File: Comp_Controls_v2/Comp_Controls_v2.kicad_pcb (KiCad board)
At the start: 2 copper layers, 78 x 108.9 mm, 39 parts

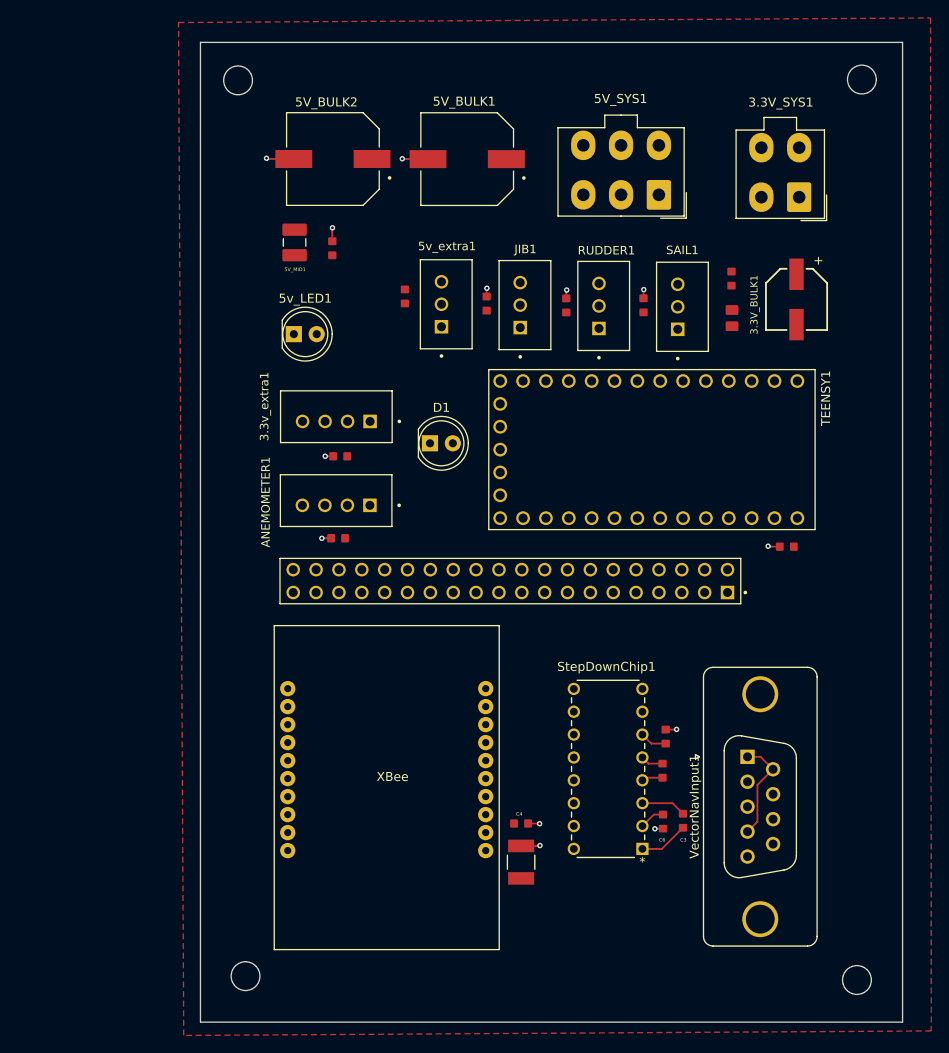
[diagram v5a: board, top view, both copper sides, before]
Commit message: rounded corners done
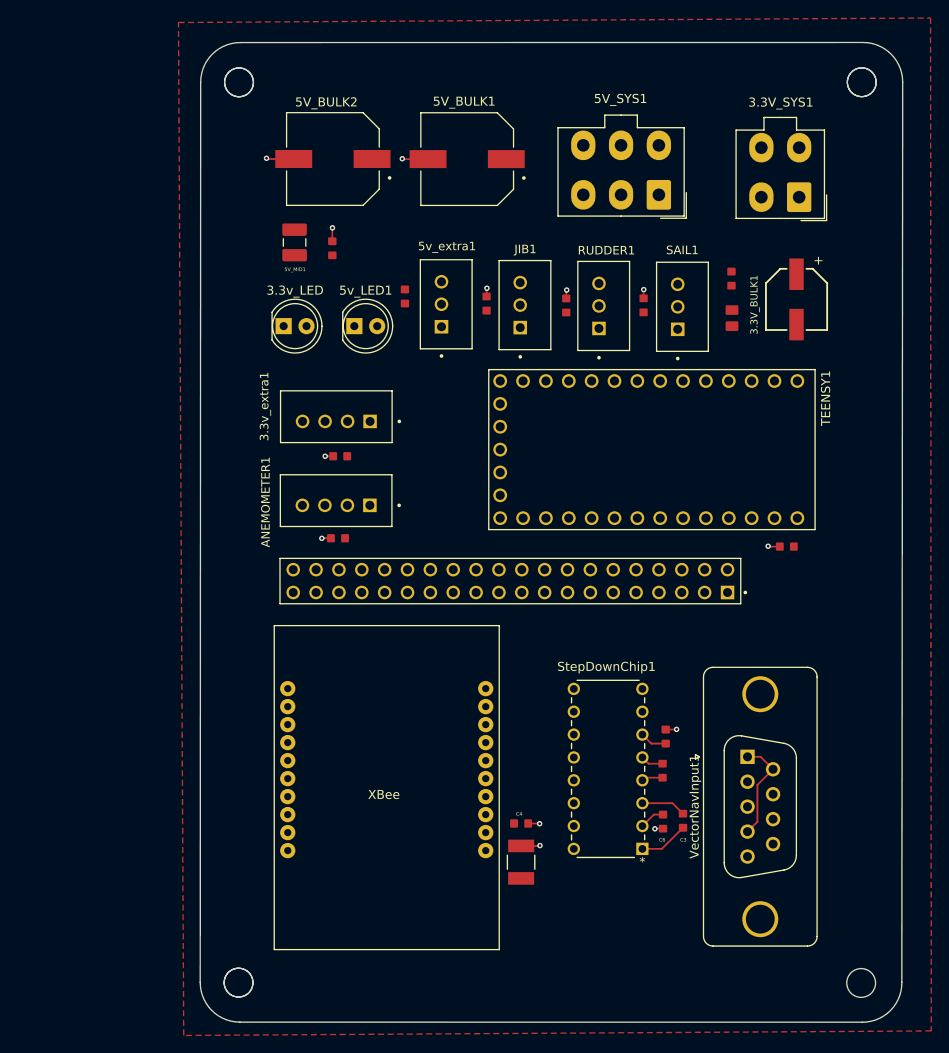
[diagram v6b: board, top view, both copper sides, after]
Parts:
- removed H2, H3, H4: MountingHole, MountingHole:MountingHole_3.2mm_M3
- added ?: , , F.Cu at (118.9, 39.5)
- added ?: , , F.Cu at (188.1, 39.5)
- added ?: , , F.Cu at (118.9, 139.5)
- added H1: MountingHole, MountingHole:MountingHole_3.2mm_M3, F.Cu at (118.9, 39.5)
- added H1: MountingHole, MountingHole:MountingHole_3.2mm_M3, F.Cu at (118.9, 139.5)
- added H1: MountingHole, MountingHole:MountingHole_3.2mm_M3, F.Cu at (188.1, 39.5)
- moved 3.3v_LED 20.8 mm to (123.9, 66.6)
- moved 5v_LED1 6.78 mm to (131.7, 66.6)
- moved H1 0.57 mm to (188.1, 139.6)
- renumbered D1 to 3.3v_LED
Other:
- board size 78 x 108.9 mm -> 78.1 x 108.9 mm

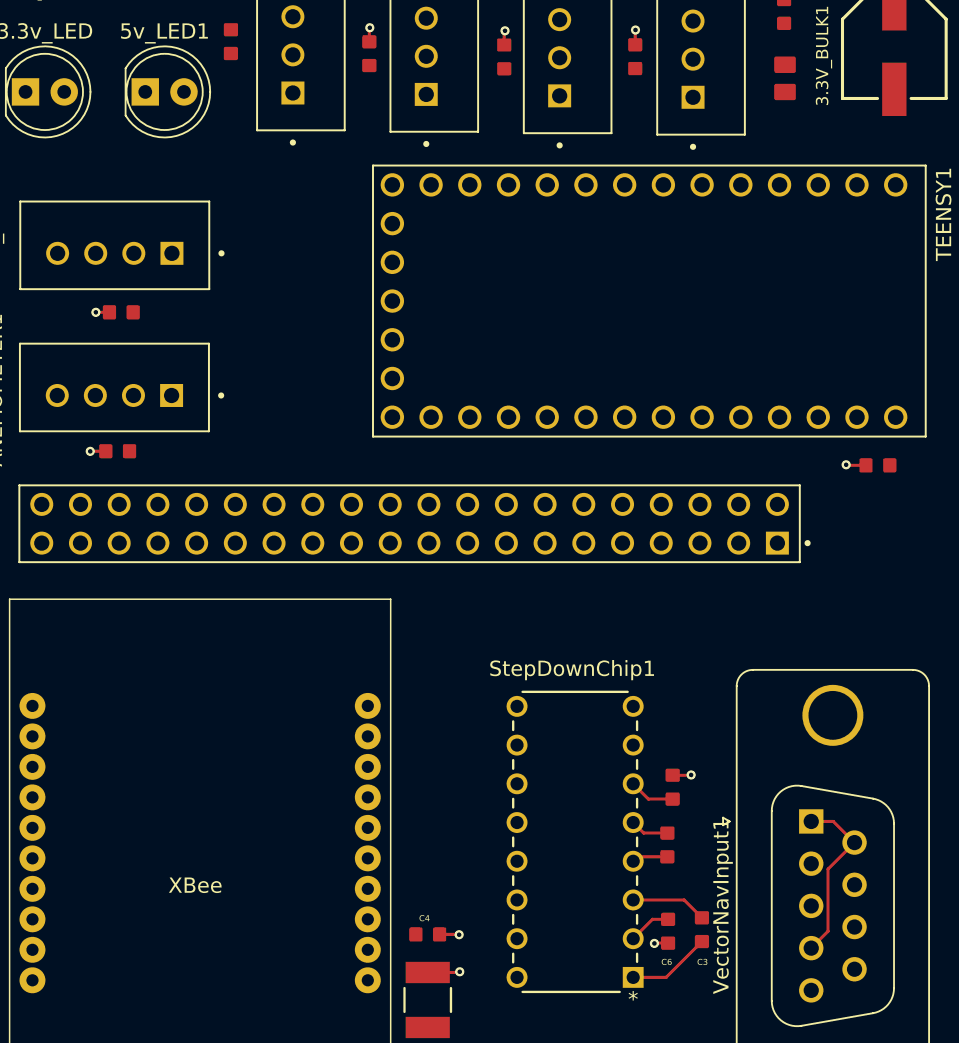
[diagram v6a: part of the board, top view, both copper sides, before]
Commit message: Add signal traces
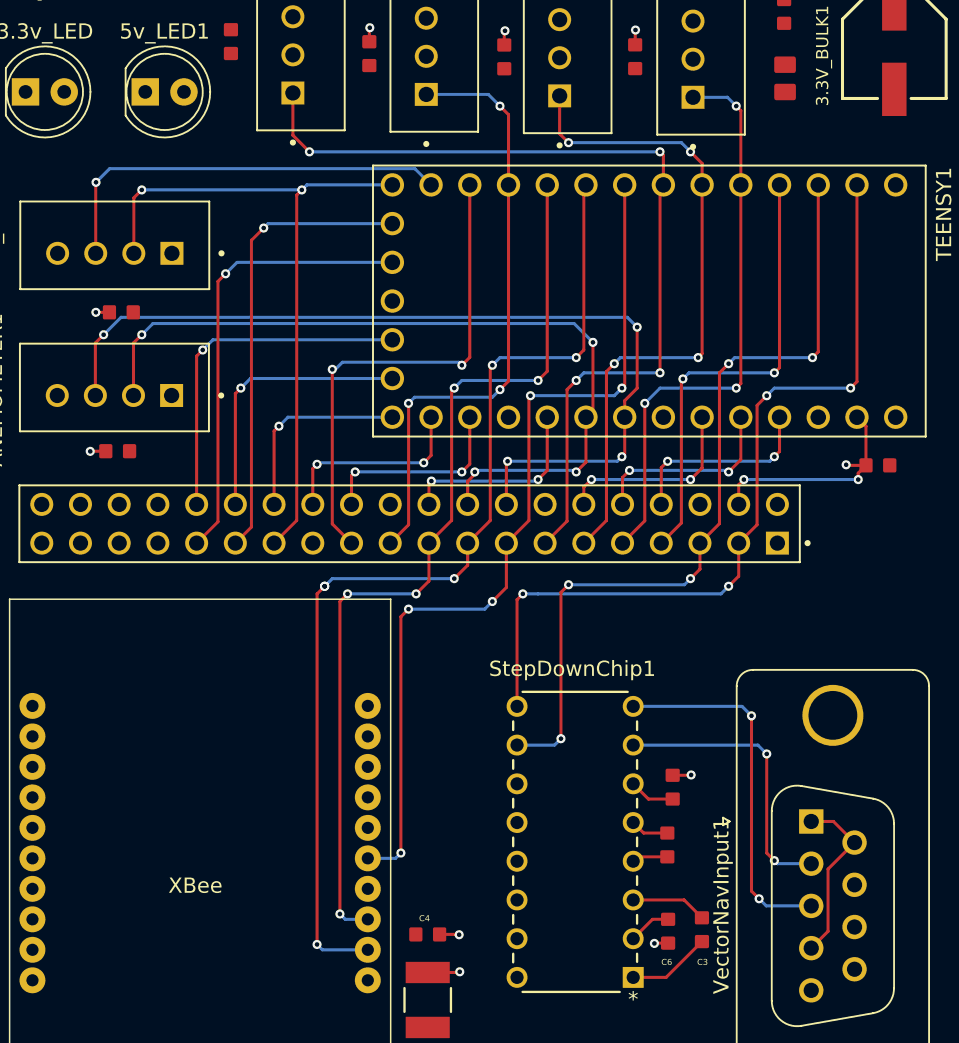
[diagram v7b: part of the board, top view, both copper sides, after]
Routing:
- net XBeeTX: track 0.00 -> 68.2 mm, vias 0 -> 6
- net XBeeRX: track 0.00 -> 61.0 mm, vias 0 -> 5
- net WindData1: track 0.00 -> 59.4 mm, vias 0 -> 4
- net 5v_extra: track 0.00 -> 59.2 mm, vias 0 -> 4
- net XBeeRESET: track 0.00 -> 58.4 mm, vias 0 -> 5
- net TeensyRX: track 0.00 -> 54.0 mm, vias 0 -> 4
- net TeensyTX: track 0.00 -> 53.8 mm, vias 0 -> 5
- net WindData0: track 0.00 -> 52.6 mm, vias 0 -> 4
- net Extra40: track 0.00 -> 44.9 mm, vias 0 -> 2
- net Rudder: track 0.00 -> 43.7 mm, vias 0 -> 4
- net JIB: track 0.00 -> 40.5 mm, vias 0 -> 3
- net Sail: track 0.00 -> 38.0 mm, vias 0 -> 3
- net 3.3v_extra: track 0.00 -> 33.0 mm, vias 0 -> 2
- net VBAT: track 0.00 -> 30.0 mm, vias 0 -> 1
- net 2: track 0.00 -> 30.0 mm, vias 0 -> 2
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
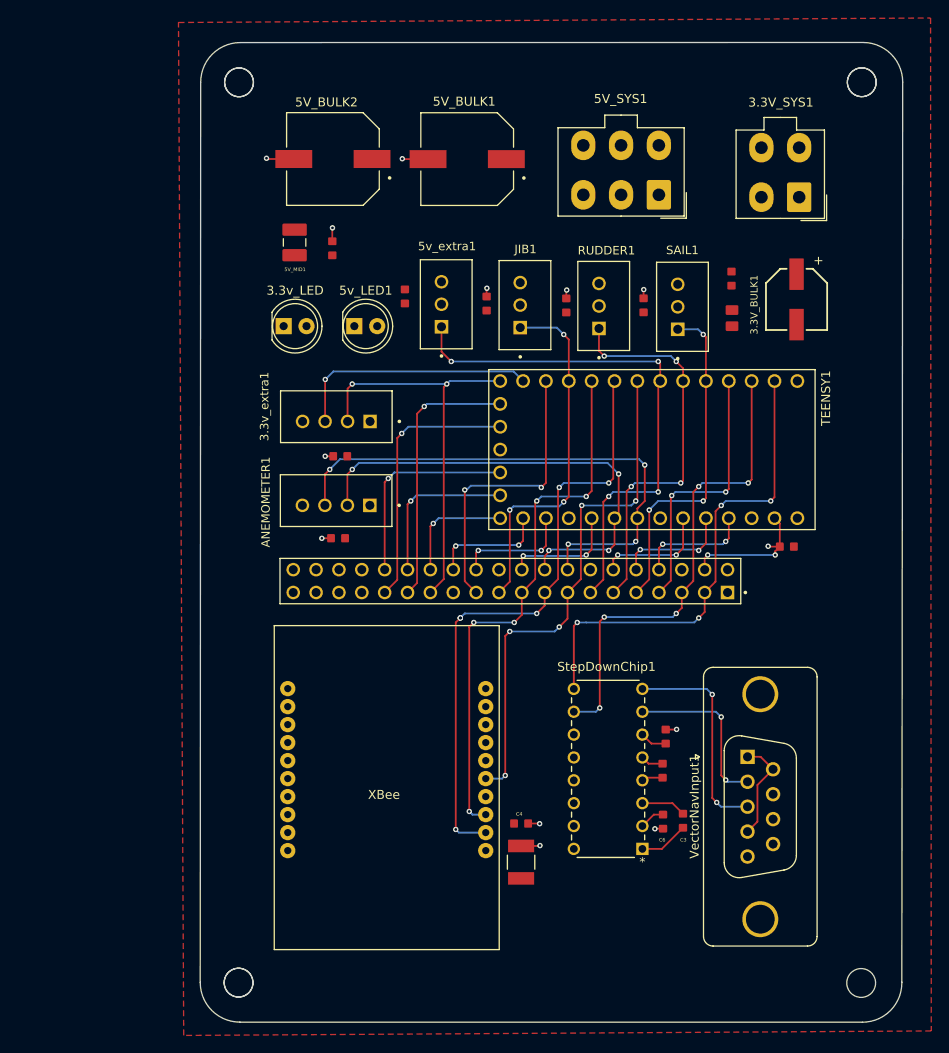
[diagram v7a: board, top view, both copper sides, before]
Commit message: remove islands, combined gnd traces with rest of system
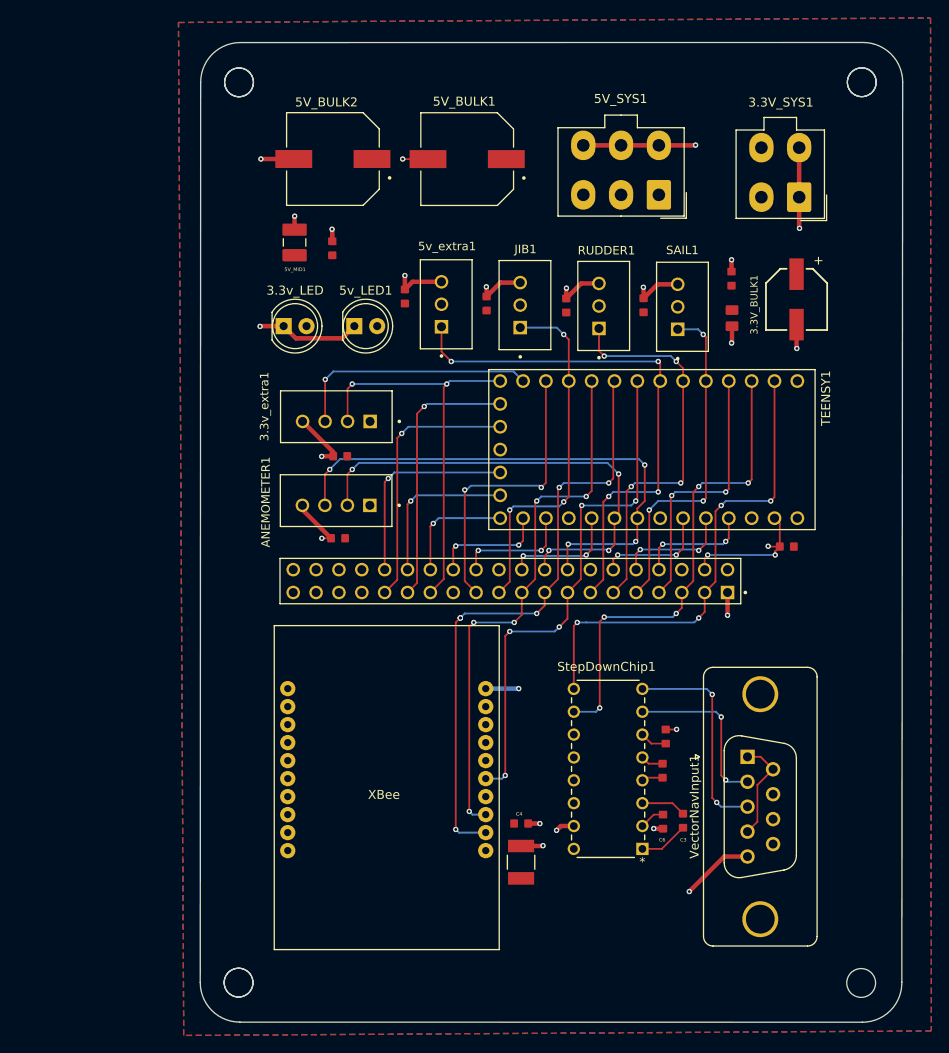
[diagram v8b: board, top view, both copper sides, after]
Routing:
- net GND: track 32.9 -> 121.0 mm, vias 15 -> 27
- added copper zone on B.Cu, net GND
- added copper zone on F.Cu, net GND
- removed copper zone on F.Cu, net (none)
